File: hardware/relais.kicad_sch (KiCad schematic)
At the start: 25 parts, among them J2 Mini XLR6, J4 Mini XLR6, J5 Mini XLR6, J6 Binder 09-0998-00-05, J7 Binder 09-0998-00-05, K1 RT314005, K10 HF49FD_005-1H12T, K11 HF49FD_005-1H12T, K12 HF49FD_005-1H12T, K13 HF49FD_005-1H12T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

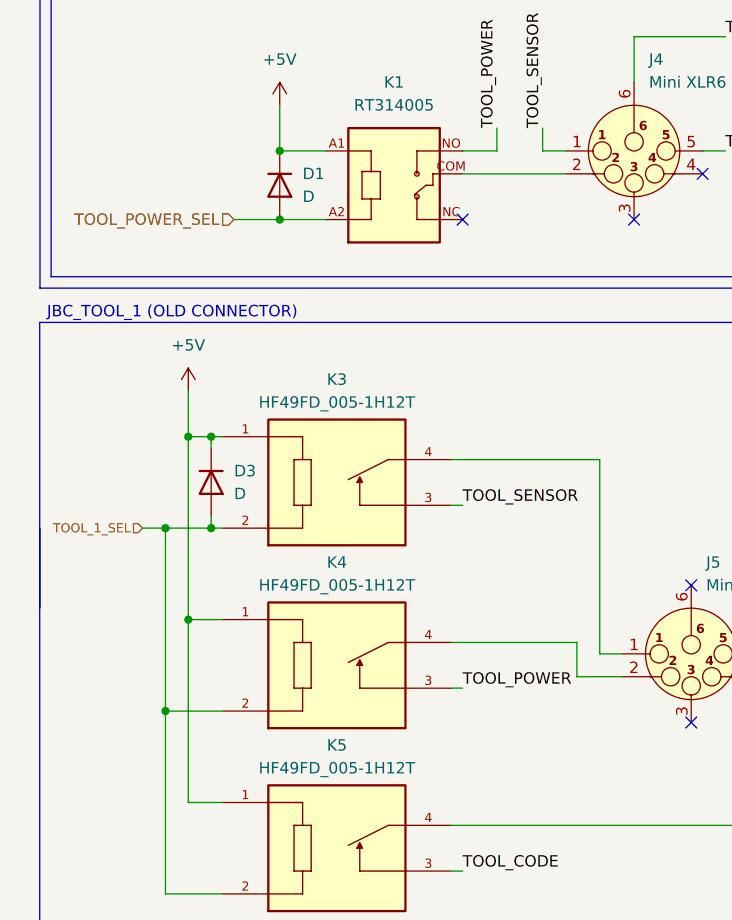
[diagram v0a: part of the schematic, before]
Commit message: Changes at Silkscreen and Gerber Files
Some cosmetic changes at PCB Silkscreen and namings in Schematic.
Gerber Files updated
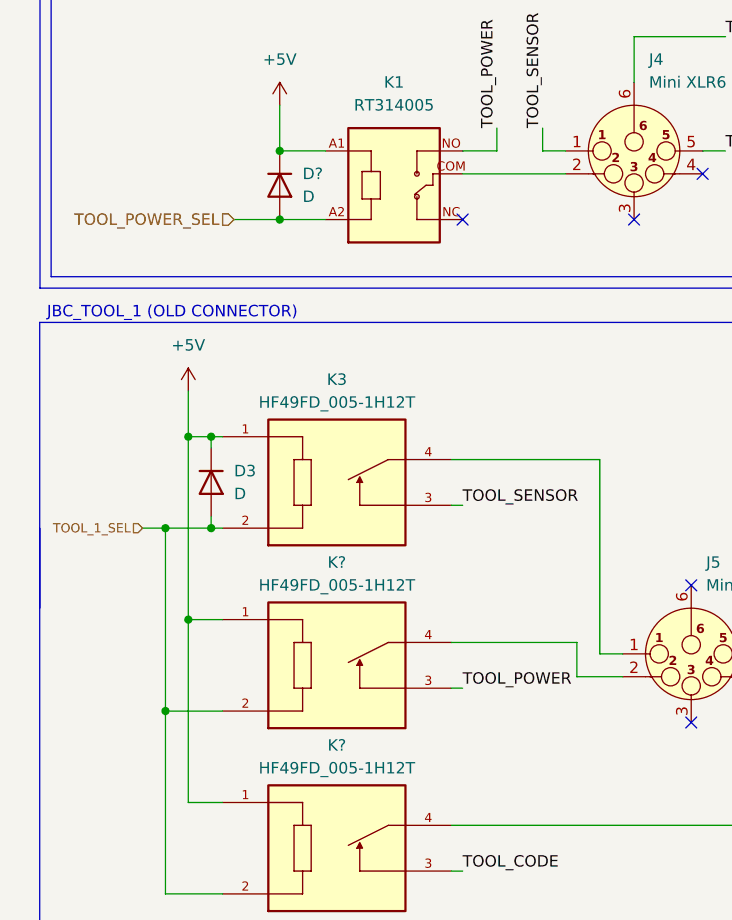
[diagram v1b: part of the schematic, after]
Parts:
- renumbered D1 to D?, K5 to K?, K4 to K?
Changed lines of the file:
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@@
 		)
 		(instances
+			(project "relais"
+				(path "/0c94c343-1f9b-49c9-b210-18156f526ae9"
+					(reference "K7")
+					(unit 1)
+				)
+			)
 			(project "JBC_Multitool"
 				(path "/e95a2ab1-77d4-4e77-b240-8651c7fb5700/154b1838-4760-485a-9d53-3854b8b8d464"
@@
 		(dnp no)
 		(fields_autoplaced yes)
-		(property "Reference" "#PWR020"
+		(property "Reference" "#PWR?"
 			(at 130.2022 29.2046 0)
 			(effects
@@
 		)
 		(instances
+			(project "relais"
+				(path "/0c94c343-1f9b-49c9-b210-18156f526ae9"
+					(reference "#PWR?")
+					(unit 1)
+				)
+			)
 			(project "JBC_Multitool"
 				(path "/e95a2ab1-77d4-4e77-b240-8651c7fb5700/154b1838-4760-485a-9d53-3854b8b8d464"
@@
 		)
 		(instances
+			(project "relais"
+				(path "/0c94c343-1f9b-49c9-b210-18156f526ae9"
+					(reference "K6")
+					(unit 1)
+				)
+			)
 			(project "JBC_Multitool"
 				(path "/e95a2ab1-77d4-4e77-b240-8651c7fb5700/154b1838-4760-485a-9d53-3854b8b8d464"
@@
 		(dnp no)
 		(fields_autoplaced yes)
-		(property "Reference" "K5"
+		(property "Reference" "K?"
 			(at 46.99 101.6 0)
 			(effects
@@
 		)
 		(instances
+			(project "relais"
+				(path "/0c94c343-1f9b-49c9-b210-18156f526ae9"
+					(reference "K?")
+					(unit 1)
+				)
+			)
 			(project "JBC_Multitool"
 				(path "/e95a2ab1-77d4-4e77-b240-8651c7fb5700/154b1838-4760-485a-9d53-3854b8b8d464"
@@
 		)
 		(instances
+			(project "relais"
+				(path "/0c94c343-1f9b-49c9-b210-18156f526ae9"
+					(reference "K8")
+					(unit 1)
+				)
+			)
 			(project "JBC_Multitool"
 				(path "/e95a2ab1-77d4-4e77-b240-8651c7fb5700/154b1838-4760-485a-9d53-3854b8b8d464"
@@
 		(dnp no)
 		(fields_autoplaced yes)
-		(property "Reference" "D1"
+		(property "Reference" "D?"
 			(at 43.18 38.0999 90)
 			(effects
@@
 		)
 		(instances
+			(project "relais"
+				(path "/0c94c343-1f9b-49c9-b210-18156f526ae9"
+					(reference "D?")
+					(unit 1)
+				)
+			)
 			(project "JBC_Multitool"
 				(path "/e95a2ab1-77d4-4e77-b240-8651c7fb5700/154b1838-4760-485a-9d53-3854b8b8d464"
@@
 		(dnp no)
 		(fields_autoplaced yes)
-		(property "Reference" "#PWR030"
+		(property "Reference" "#PWR?"
 			(at 115.57 66.04 0)
 			(effects
@@
 		)
 		(instances
+			(project "relais"
+				(path "/0c94c343-1f9b-49c9-b210-18156f526ae9"
+					(reference "#PWR?")
+					(unit 1)
+				)
+			)
 			(project "JBC_Multitool"
 				(path "/e95a2ab1-77d4-4e77-b240-8651c7fb5700/154b1838-4760-485a-9d53-3854b8b8d464"
@@
 		)
 		(instances
+			(project "relais"
+				(path "/0c94c343-1f9b-49c9-b210-18156f526ae9"
+					(reference "K1")
+					(unit 1)
+				)
+			)
 			(project "JBC_Multitool"
 				(path "/e95a2ab1-77d4-4e77-b240-8651c7fb5700/154b1838-4760-485a-9d53-3854b8b8d464"
@@
 		)
 		(instances
+			(project "relais"
+				(path "/0c94c343-1f9b-49c9-b210-18156f526ae9"
+					(reference "J2")
+					(unit 1)
+				)
+			)
 			(project "JBC_Multitool"
 				(path "/e95a2ab1-77d4-4e77-b240-8651c7fb5700/154b1838-4760-485a-9d53-3854b8b8d464"
@@
 		)
 		(instances
+			(project "relais"
+				(path "/0c94c343-1f9b-49c9-b210-18156f526ae9"
+					(reference "D5")
+					(unit 1)
+				)
+			)
 			(project "JBC_Multitool"
 				(path "/e95a2ab1-77d4-4e77-b240-8651c7fb5700/154b1838-4760-485a-9d53-3854b8b8d464"
@@
 		)
 		(instances
+			(project "relais"
+				(path "/0c94c343-1f9b-49c9-b210-18156f526ae9"
+					(reference "D3")
+					(unit 1)
+				)
+			)
 			(project "JBC_Multitool"
 				(path "/e95a2ab1-77d4-4e77-b240-8651c7fb5700/154b1838-4760-485a-9d53-3854b8b8d464"
@@
 		)
 		(instances
+			(project "relais"
+				(path "/0c94c343-1f9b-49c9-b210-18156f526ae9"
+					(reference "J4")
+					(unit 1)
+				)
+			)
 			(project "JBC_Multitool"
 				(path "/e95a2ab1-77d4-4e77-b240-8651c7fb5700/154b1838-4760-485a-9d53-3854b8b8d464"
@@
 		(dnp no)
 		(fields_autoplaced yes)
-		(property "Reference" "#PWR022"
+		(property "Reference" "#PWR?"
 			(at 200.66 66.04 0)
 			(effects
@@
 		)
 		(instances
+			(project "relais"
+				(path "/0c94c343-1f9b-49c9-b210-18156f526ae9"
+					(reference "#PWR?")
+					(unit 1)
+				)
+			)
 			(project "JBC_Multitool"
 				(path "/e95a2ab1-77d4-4e77-b240-8651c7fb5700/154b1838-4760-485a-9d53-3854b8b8d464"
@@
 		(dnp no)
 		(fields_autoplaced yes)
-		(property "Reference" "K4"
+		(property "Reference" "K?"
 			(at 46.99 81.28 0)
 			(effects
@@
 		)
 		(instances
+			(project "relais"
+				(path "/0c94c343-1f9b-49c9-b210-18156f526ae9"
+					(reference "K?")
+					(unit 1)
+				)
+			)
 			(project "JBC_Multitool"
 				(path "/e95a2ab1-77d4-4e77-b240-8651c7fb5700/154b1838-4760-485a-9d53-3854b8b8d464"
@@
 		)
 		(instances
+			(project "relais"
+				(path "/0c94c343-1f9b-49c9-b210-18156f526ae9"
+					(reference "J7")
+					(unit 1)
+				)
+			)
 			(project "JBC_Multitool"
 				(path "/e95a2ab1-77d4-4e77-b240-8651c7fb5700/154b1838-4760-485a-9d53-3854b8b8d464"
@@
 		)
 		(instances
+			(project "relais"
+				(path "/0c94c343-1f9b-49c9-b210-18156f526ae9"
+					(reference "K12")
+					(unit 1)
+				)
+			)
 			(project "JBC_Multitool"
 				(path "/e95a2ab1-77d4-4e77-b240-8651c7fb5700/154b1838-4760-485a-9d53-3854b8b8d464"
@@
 		)
 		(instances
+			(project "relais"
+				(path "/0c94c343-1f9b-49c9-b210-18156f526ae9"
+					(reference "K14")
+					(unit 1)
+				)
+			)
 			(project "JBC_Multitool"
 				(path "/e95a2ab1-77d4-4e77-b240-8651c7fb5700/154b1838-4760-485a-9d53-3854b8b8d464"
@@
 		(dnp no)
 		(fields_autoplaced yes)
-		(property "Reference" "#PWR023"
+		(property "Reference" "#PWR?"
 			(at 30.48 135.89 0)
 			(effects
@@
 		)
 		(instances
+			(project "relais"
+				(path "/0c94c343-1f9b-49c9-b210-18156f526ae9"
+					(reference "#PWR?")
+					(unit 1)
+				)
+			)
 			(project "JBC_Multitool"
 				(path "/e95a2ab1-77d4-4e77-b240-8651c7fb5700/154b1838-4760-485a-9d53-3854b8b8d464"
@@
 		(dnp no)
 		(fields_autoplaced yes)
-		(property "Reference" "#PWR021"
+		(property "Reference" "#PWR?"
 			(at 30.48 66.04 0)
 			(effects
@@
 		)
 		(instances
+			(project "relais"
+				(path "/0c94c343-1f9b-49c9-b210-18156f526ae9"
+					(reference "#PWR?")
+					(unit 1)
+				)
+			)
 			(project "JBC_Multitool"
 				(path "/e95a2ab1-77d4-4e77-b240-8651c7fb5700/154b1838-4760-485a-9d53-3854b8b8d464"
@@
 		)
 		(instances
+			(project "relais"
+				(path "/0c94c343-1f9b-49c9-b210-18156f526ae9"
+					(reference "D4")
+					(unit 1)
+				)
+			)
 			(project "JBC_Multitool"
 				(path "/e95a2ab1-77d4-4e77-b240-8651c7fb5700/154b1838-4760-485a-9d53-3854b8b8d464"
@@
 		)
 		(instances
+			(project "relais"
+				(path "/0c94c343-1f9b-49c9-b210-18156f526ae9"
+					(reference "D2")
+					(unit 1)
+				)
+			)
 			(project ""
 				(path "/e95a2ab1-77d4-4e77-b240-8651c7fb5700/154b1838-4760-485a-9d53-3854b8b8d464"
@@
 		)
 		(instances
+			(project "relais"
+				(path "/0c94c343-1f9b-49c9-b210-18156f526ae9"
+					(reference "K9")
+					(unit 1)
+				)
+			)
 			(project "JBC_Multitool"
 				(path "/e95a2ab1-77d4-4e77-b240-8651c7fb5700/154b1838-4760-485a-9d53-3854b8b8d464"
@@
 		)
 		(instances
+			(project "relais"
+				(path "/0c94c343-1f9b-49c9-b210-18156f526ae9"
+					(reference "K11")
+					(unit 1)
+				)
+			)
 			(project "JBC_Multitool"
 				(path "/e95a2ab1-77d4-4e77-b240-8651c7fb5700/154b1838-4760-485a-9d53-3854b8b8d464"
@@
 		)
 		(instances
+			(project "relais"
+				(path "/0c94c343-1f9b-49c9-b210-18156f526ae9"
+					(reference "K13")
+					(unit 1)
+				)
+			)
 			(project "JBC_Multitool"
 				(path "/e95a2ab1-77d4-4e77-b240-8651c7fb5700/154b1838-4760-485a-9d53-3854b8b8d464"
@@
 		)
 		(instances
+			(project "relais"
+				(path "/0c94c343-1f9b-49c9-b210-18156f526ae9"
+					(reference "D6")
+					(unit 1)
+				)
+			)
 			(project "JBC_Multitool"
 				(path "/e95a2ab1-77d4-4e77-b240-8651c7fb5700/154b1838-4760-485a-9d53-3854b8b8d464"
@@
 		)
 		(instances
+			(project "relais"
+				(path "/0c94c343-1f9b-49c9-b210-18156f526ae9"
+					(reference "K10")
+					(unit 1)
+				)
+			)
 			(project "JBC_Multitool"
 				(path "/e95a2ab1-77d4-4e77-b240-8651c7fb5700/154b1838-4760-485a-9d53-3854b8b8d464"
@@
 		)
 		(instances
+			(project "relais"
+				(path "/0c94c343-1f9b-49c9-b210-18156f526ae9"
+					(reference "J5")
+					(unit 1)
+				)
+			)
 			(project "JBC_Multitool"
 				(path "/e95a2ab1-77d4-4e77-b240-8651c7fb5700/154b1838-4760-485a-9d53-3854b8b8d464"
@@
 		)
 		(instances
+			(project "relais"
+				(path "/0c94c343-1f9b-49c9-b210-18156f526ae9"
+					(reference "J6")
+					(unit 1)
+				)
+			)
 			(project ""
 				(path "/e95a2ab1-77d4-4e77-b240-8651c7fb5700/154b1838-4760-485a-9d53-3854b8b8d464"
@@
 		(dnp no)
 		(fields_autoplaced yes)
-		(property "Reference" "#PWR019"
+		(property "Reference" "#PWR?"
 			(at 40.64 34.29 0)
 			(effects
@@
 		)
 		(instances
+			(project "relais"
+				(path "/0c94c343-1f9b-49c9-b210-18156f526ae9"
+					(reference "#PWR?")
+					(unit 1)
+				)
+			)
 			(project "JBC_Multitool"
 				(path "/e95a2ab1-77d4-4e77-b240-8651c7fb5700/154b1838-4760-485a-9d53-3854b8b8d464"
@@
 		)
 		(instances
+			(project "relais"
+				(path "/0c94c343-1f9b-49c9-b210-18156f526ae9"
+					(reference "K3")
+					(unit 1)
+				)
+			)
 			(project "JBC_Multitool"
 				(path "/e95a2ab1-77d4-4e77-b240-8651c7fb5700/154b1838-4760-485a-9d53-3854b8b8d464"
@@
 		)
 		(instances
+			(project "relais"
+				(path "/0c94c343-1f9b-49c9-b210-18156f526ae9"
+					(reference "K2")
+					(unit 1)
+				)
+			)
 			(project "JBC_Multitool"
 				(path "/e95a2ab1-77d4-4e77-b240-8651c7fb5700/154b1838-4760-485a-9d53-3854b8b8d464"
@@
 		)
 	)
+	(sheet_instances
+		(path "/"
+			(page "1")
+		)
+	)
+	(embedded_fonts no)
 )
